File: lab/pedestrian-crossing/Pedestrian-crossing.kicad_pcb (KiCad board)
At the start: 2 copper layers, 80 x 110 mm, 13 parts, among them U1 atmega328p

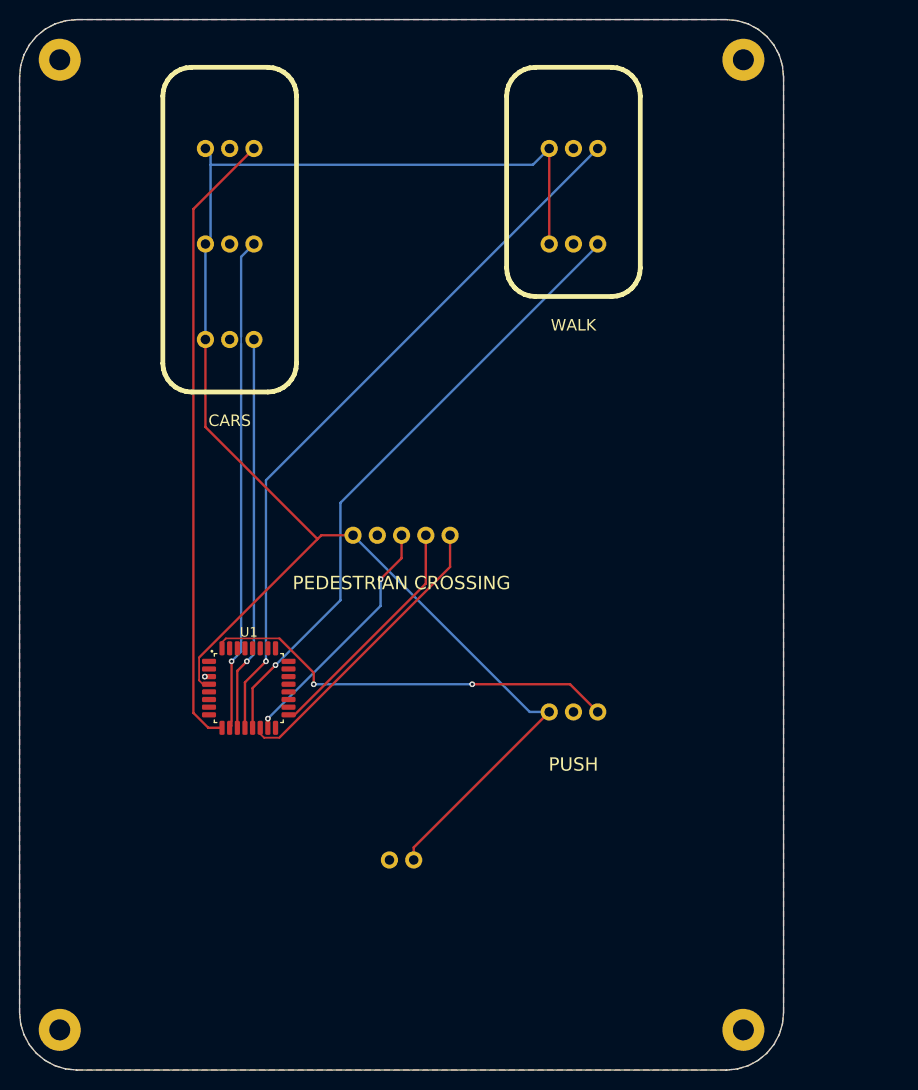
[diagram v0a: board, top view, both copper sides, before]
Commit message: lab: every board is a real board: an Arduino Nano and registry parts, routed, ready to order
The lab boards ran on simulation-only envelopes (labMcu, labDisplay, a battery). Now each is
an Arduino Nano on two sockets on the back (flashed over its USB, the image the app builds),
its lights LEDs through 1 kΩ, its knobs PTV09A pots, its display the MAX7219 eight-digit
module, its sensors an SHT31 and an SCD40 with their datasheets' support circuits, the FTDI
header for the serial console; the servo boards take 5 V on a screw terminal with a bulk
capacitor. All ten check complete with no errors or warnings, their firmware unchanged
(serial-device now on the 328P), and run in the lab without a fault (3 s each, dev host).

The registry: every interactive board must be ready to order and flash (publish.mjs refuses
one that is not; status simulation-only removed).

Claude-Session: https://claude.ai/code/session_01ATmMmxyrWxFwR3nTdXUrcx
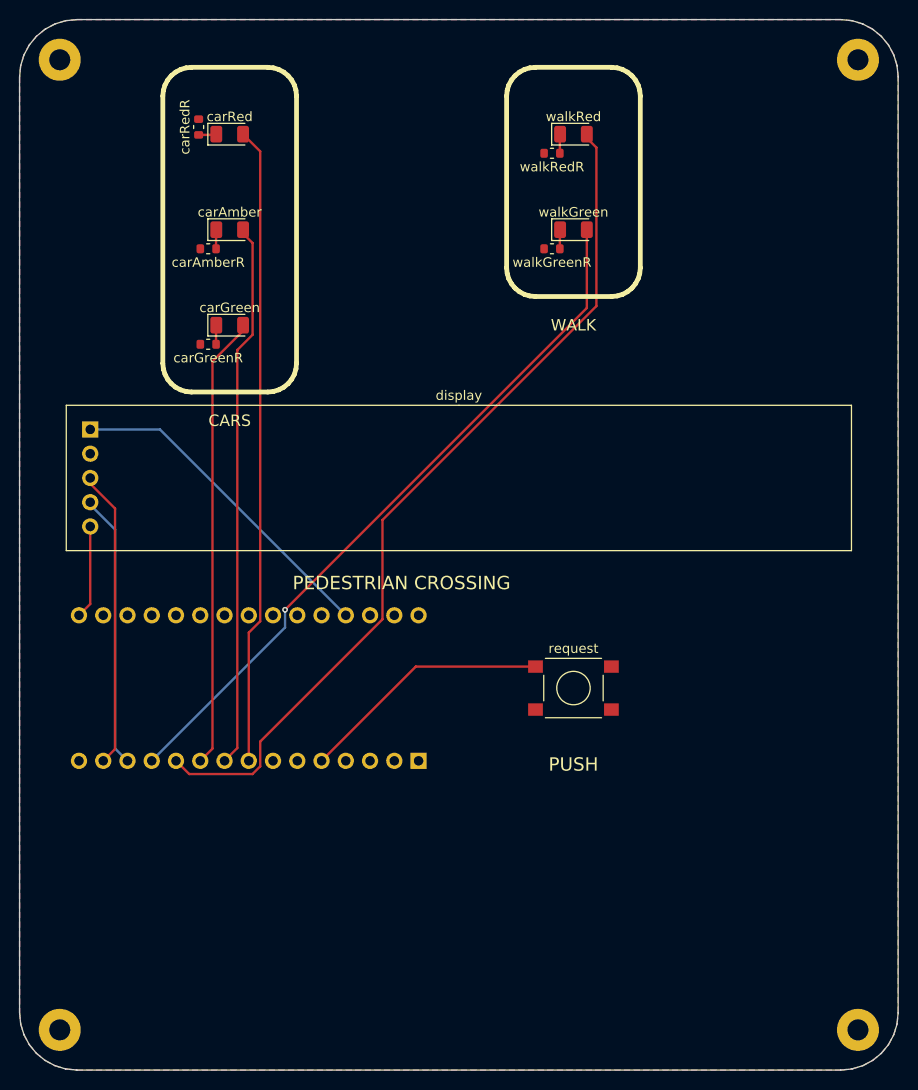
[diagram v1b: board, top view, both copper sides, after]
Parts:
- removed battery: battery, Regulated battery module
- removed the carAmber at (122.0, 112.0)
- removed the carGreen at (122.0, 122.0)
- removed the carRed at (122.0, 102.0)
- removed the display at (140.0, 138.0)
- removed the request at (158.0, 160.0)
- removed the walkGreen at (158.0, 112.0)
- removed the walkRed at (158.0, 102.0)
- added carAmber: orange, LED_1206_3216Metric, F.Cu at (122.0, 112.0)
- added carAmberR: 1kohm, R_0603_1608Metric, F.Cu at (119.8, 114.0)
- added carGreen: green, LED_1206_3216Metric, F.Cu at (122.0, 122.0)
- added carGreenR: 1kohm, R_0603_1608Metric, F.Cu at (119.8, 124.0)
- added carRed: red, LED_1206_3216Metric, F.Cu at (122.0, 102.0)
- added carRedR: 1kohm, R_0603_1608Metric, F.Cu at (118.8, 101.2)
- added display: MAX7219 8-digit 7-segment LED display module, MAX7219_8digit_Module_Socket_1x05_P2.54mm, F.Cu at (146.0, 138.0)
- added request: PTS645SM43SMTR92 LFS, SW_Tactile_SPST_6x6mm_SMD, F.Cu at (158.0, 160.0)
- added walkGreen: green, LED_1206_3216Metric, F.Cu at (158.0, 112.0)
- added walkGreenR: 1kohm, R_0603_1608Metric, F.Cu at (155.8, 114.0)
- added walkRed: red, LED_1206_3216Metric, F.Cu at (158.0, 102.0)
- added walkRedR: 1kohm, R_0603_1608Metric, F.Cu at (155.8, 104.0)
- U1: value atmega328p -> A000005; footprint TQFP-32_7x7mm_P0.8mm -> Arduino_Nano_Socket_2x15_P2.54mm_W15.24mm; moved to B.Cu
- moved H2 12.0 mm to (187.8, 195.8)
- moved H3 12.0 mm to (187.8, 94.2)
- turned U1 to 90 degrees
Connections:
- U1 pad 10: CAR_AMBER -> CAR_GREEN
- U1 pad 11: CAR_GREEN -> WALK_RED
- U1 pad 12: WALK_RED -> WALK_GREEN
- U1 pad 13: WALK_GREEN -> LOAD
- U1 pad 14: LOAD -> MOSI
- U1 pad 15: MOSI -> (no net)
- U1 pad 16: (no net) -> SCK
- U1 pad 17: SCK -> (no net)
- U1 pad 27: (no net) -> V5
- U1 pad 29: (no net) -> GND
- U1 pad 3: GND -> (no net)
- U1 pad 4: V5 -> GND
- U1 pad 5: (no net) -> REQUEST
- U1 pad 8: (no net) -> CAR_RED
- U1 pad 9: CAR_RED -> CAR_AMBER
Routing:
- net V5: track 165.1 -> 34.8 mm
- net REQUEST: track 44.0 -> 26.5 mm, vias 2 -> 0
- net SCK: track 25.1 -> 9.79 mm
- net WALK_RED: track 76.0 -> 90.9 mm, vias 1 -> 0
- net WALK_GREEN: track 65.6 -> 74.5 mm
- net CAR_GREEN: track 41.4 -> 47.5 mm, vias 1 -> 0
- net CAR_AMBER: track 51.7 -> 57.3 mm, vias 1 -> 0
- net MOSI: track 26.0 -> 31.2 mm, vias 2 -> 0
- net LOAD: track 31.4 -> 28.7 mm
- net CAR_RED_K: track 0.00 -> 2.09 mm
- net WALK_RED_K: track 0.00 -> 2.08 mm
- net WALK_GREEN_K: track 0.00 -> 2.01 mm
- net CAR_GREEN_K: track 0.00 -> 2.01 mm
- net CAR_AMBER_K: track 0.00 -> 2.01 mm
- net CAR_RED: track 65.4 -> 66.9 mm
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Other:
- board size 80 x 110 mm -> 92 x 110 mm

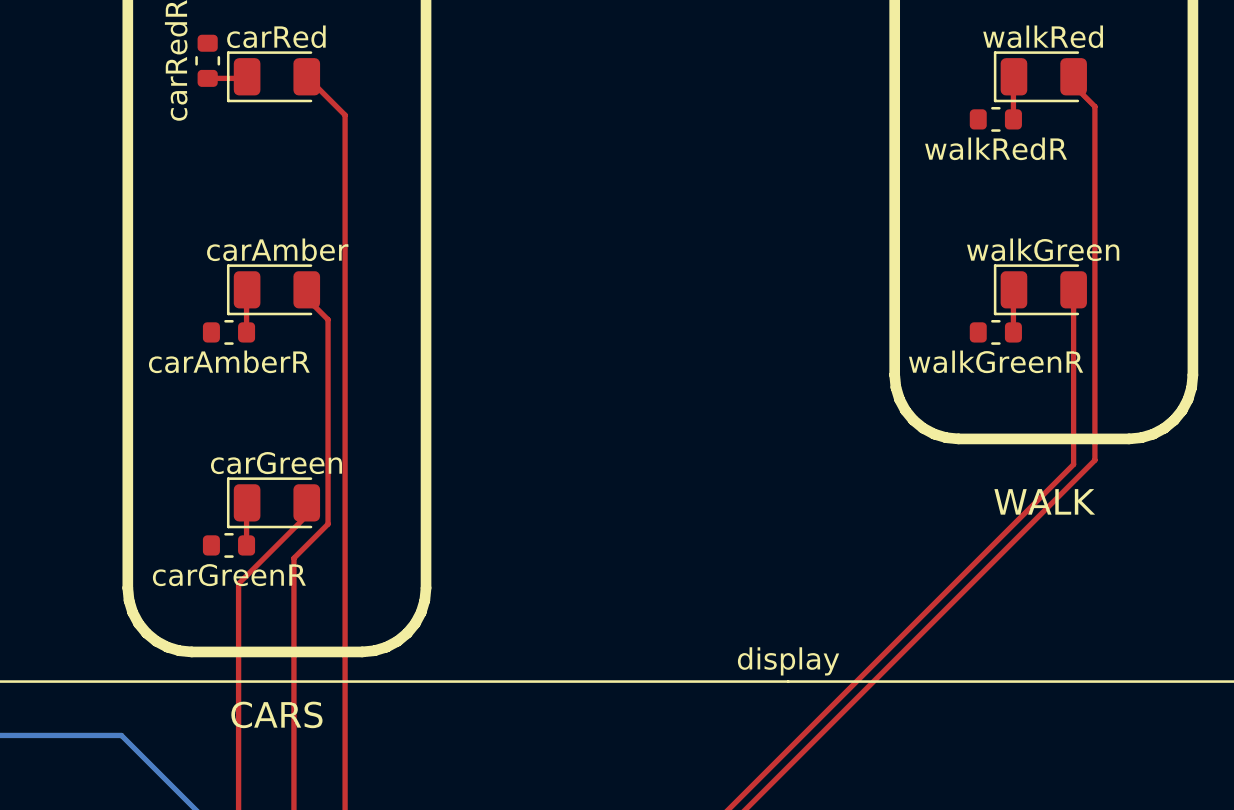
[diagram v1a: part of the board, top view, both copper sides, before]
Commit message: registry: every board rebuilt with pcbkit main 4684674e6 - the bought part named on the board
pcbkit dc07fdfd6 writes the bought row's MPN and Manufacturer (the design's own kept as DesignMPN /
DesignManufacturer) and the build chooses parts before it places (6361ec104). Each of the 44 boards
was rebuilt (; the two P4 boards  only: their builds reroute pairs):
copper unchanged on all 44 (segments, arcs and vias counted before and after), placement kept; the
Arduino and lab boards now carry the parts the catalogue gives them. The check gains only the new
judgements: part-maker (a part bought from another maker) and part-missing on hand-fitted modules
(DS1 sockets); p4-touch-7 loses part-stale. The P4 boards keep their hole-clearance errors (a
reroute is Team 3's).

Claude-Session: https://claude.ai/code/session_01BAgp959tApA8aEg85EYgfb
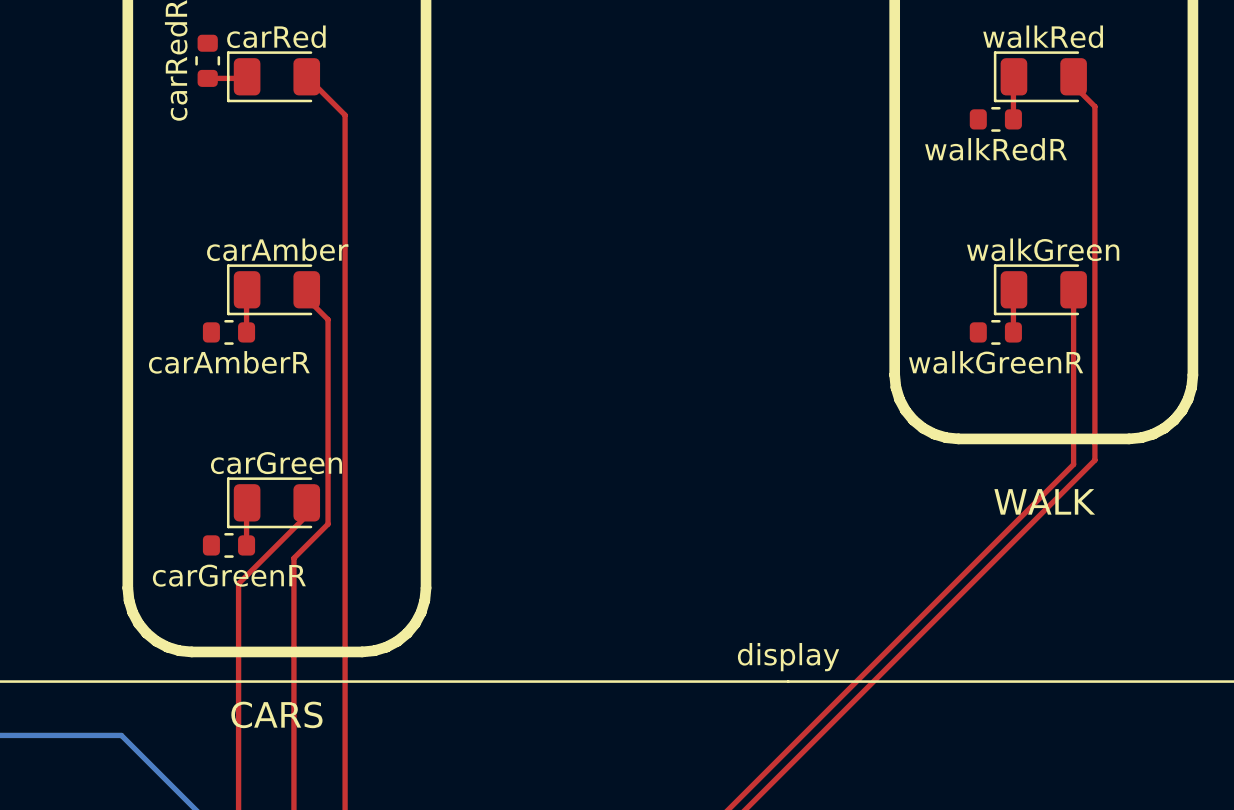
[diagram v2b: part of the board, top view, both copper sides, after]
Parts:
- H1, H2, H3, H4: value (none) -> MountingHole_2.2mm_M2_Pad
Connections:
- request pad 2: REQUEST -> GND
